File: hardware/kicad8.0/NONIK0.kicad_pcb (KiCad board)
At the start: 2 copper layers, 55 x 22 mm, 23 parts, among them J1 AVR-UPDI-3, J2 Qwiic/Stemma QT, J3 Test Pads, SW1 SW_SPST, SW2 SW_Push, SW3 SW_Push, U1 LED_HCMS-2915, U2 ATtiny1604-SS, U3 AP3602A

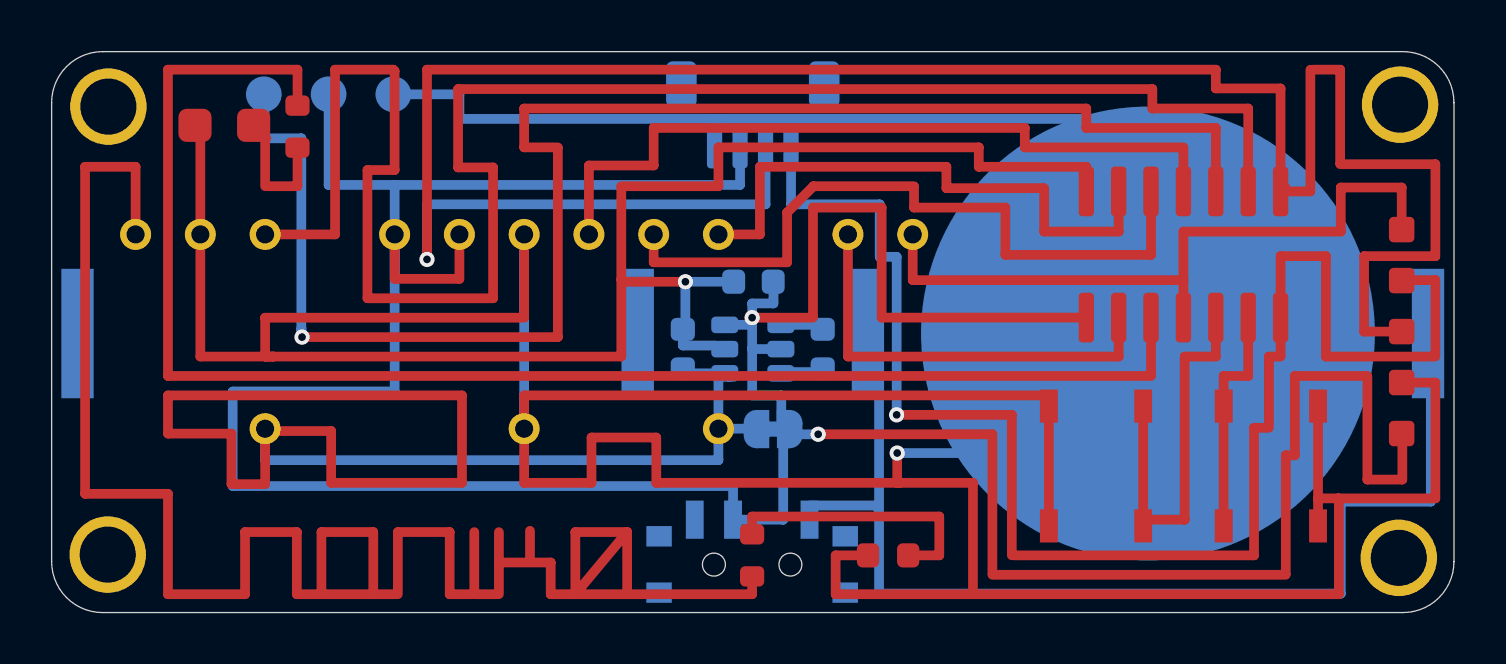
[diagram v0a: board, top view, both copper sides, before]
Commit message: more test pads
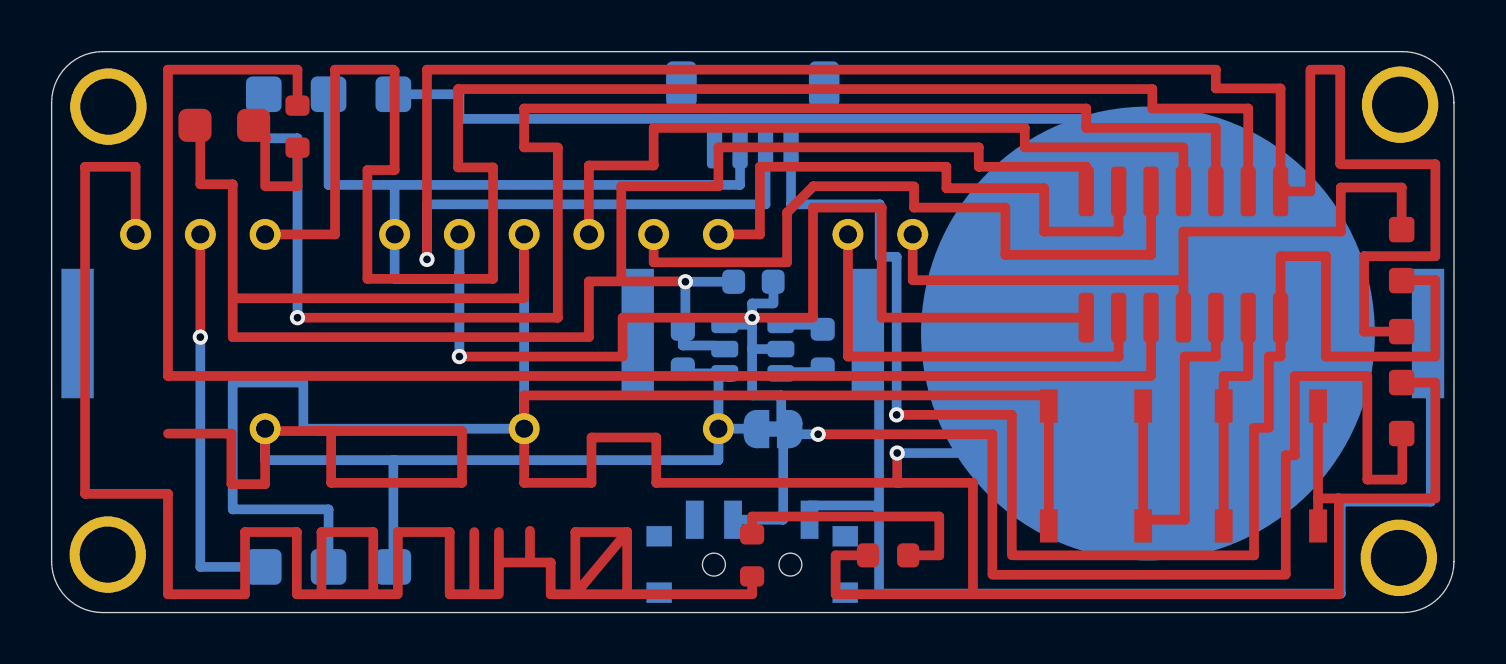
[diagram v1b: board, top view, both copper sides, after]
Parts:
- added J4: Test Pads, NONIK0:Pads_1x3_2.54mm, B.Cu at (51.2, 37.8)
- J1: footprint NONIK0:UPDI_Pads -> NONIK0:Pads_1x3_2.54mm
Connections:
- U1 pad 25: GND -> OSC
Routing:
- net GND: track 251.1 -> 272.5 mm
- net VCC: track 148.3 -> 127.3 mm, vias 2 -> 3
- net OSC: track 0.00 -> 15.5 mm, vias 0 -> 1
- net Vled: track 59.9 -> 55.4 mm
- net UPDI: track 62.0 -> 59.8 mm
- net RESET: track 71.1 -> 69.6 mm
